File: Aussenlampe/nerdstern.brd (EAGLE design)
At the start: 60 x 50 mm, 14 parts, among them K1 G6RS

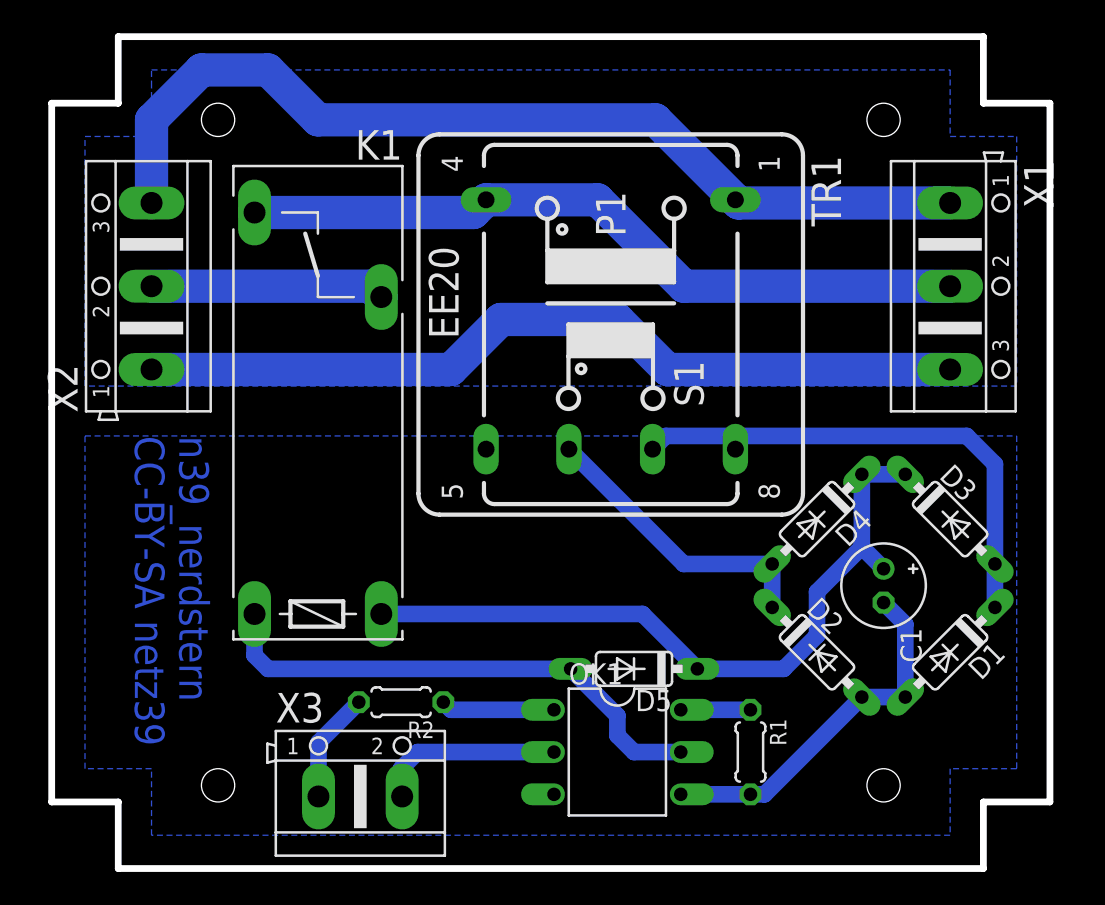
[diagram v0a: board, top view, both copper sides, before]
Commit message: modified .gitignore
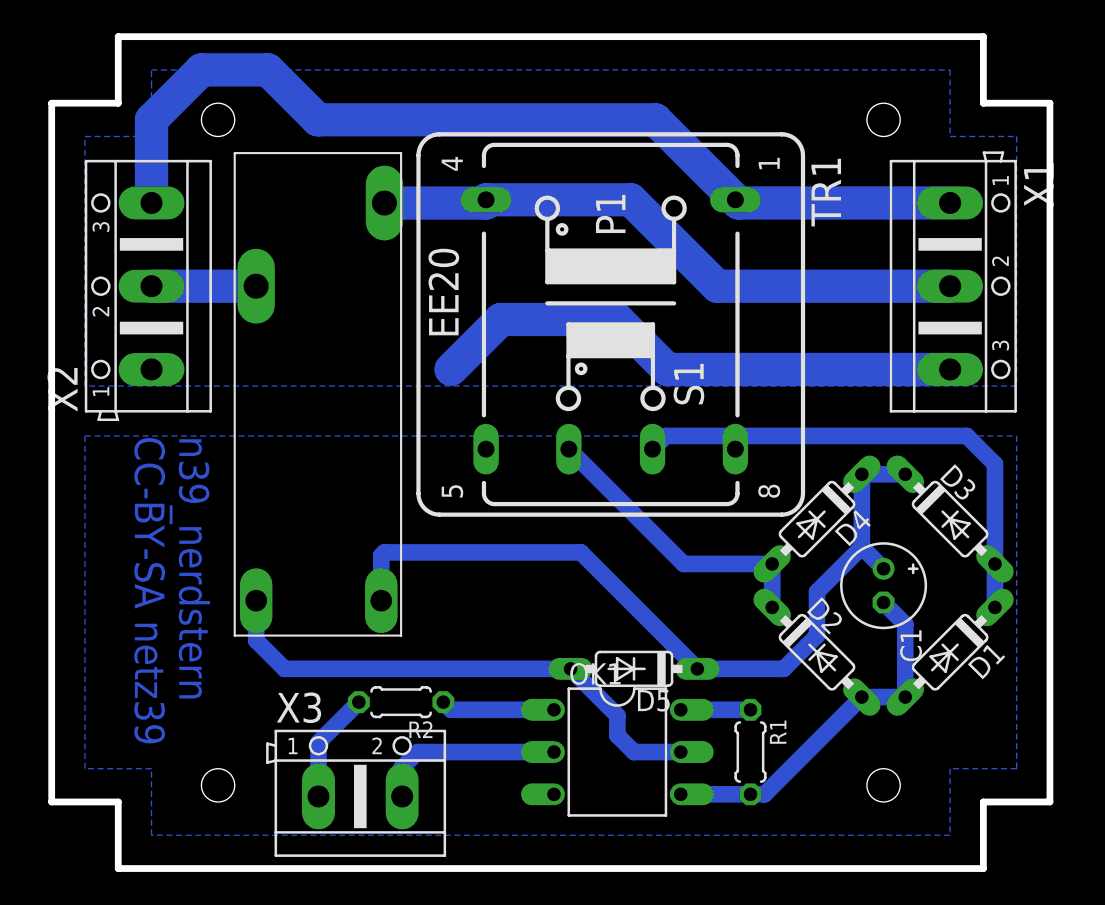
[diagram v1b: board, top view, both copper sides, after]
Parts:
- removed K1: G6RS, relay:G6RS
- added U$1: JS_05_MN_KT, n39:JS_05_MN_KT
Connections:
- removed net N$12: D5.A, K1.2, OK1.5
- new net N$6: D5.A, OK1.5, U$1.P$2
- net N$1: now also U$1.P$4; no longer K1.S
- net N$2: now also U$1.P$3; no longer K1.P
- net N$5: now also U$1.P$1; no longer K1.1
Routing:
- net N$6: track 0.00 -> 31.4 mm
- net N$12: track 31.2 -> 0.00 mm
- net GND2: track 50.5 -> 32.5 mm
- net N$1: track 44.3 -> 36.3 mm
- net N$2: track 14.1 -> 6.29 mm
- net N$5: track 43.7 -> 48.0 mm
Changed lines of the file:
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@@
 <layer number="27" name="tValues" color="7" fill="1" visible="yes" active="yes"/>
 <layer number="28" name="bValues" color="7" fill="1" visible="yes" active="yes"/>
-<layer number="29" name="tStop" color="7" fill="3" visible="no" active="yes"/>
-<layer number="30" name="bStop" color="7" fill="6" visible="no" active="yes"/>
-<layer number="31" name="tCream" color="7" fill="4" visible="no" active="yes"/>
-<layer number="32" name="bCream" color="7" fill="5" visible="no" active="yes"/>
-<layer number="33" name="tFinish" color="6" fill="3" visible="no" active="yes"/>
-<layer number="34" name="bFinish" color="6" fill="6" visible="no" active="yes"/>
-<layer number="35" name="tGlue" color="7" fill="4" visible="no" active="yes"/>
-<layer number="36" name="bGlue" color="7" fill="5" visible="no" active="yes"/>
-<layer number="37" name="tTest" color="7" fill="1" visible="no" active="yes"/>
-<layer number="38" name="bTest" color="7" fill="1" visible="no" active="yes"/>
-<layer number="39" name="tKeepout" color="4" fill="11" visible="no" active="yes"/>
-<layer number="40" name="bKeepout" color="1" fill="11" visible="no" active="yes"/>
-<layer number="41" name="tRestrict" color="4" fill="10" visible="no" active="yes"/>
-<layer number="42" name="bRestrict" color="1" fill="10" visible="no" active="yes"/>
-<layer number="43" name="vRestrict" color="2" fill="10" visible="no" active="yes"/>
+<layer number="29" name="tStop" color="7" fill="3" visible="yes" active="yes"/>
+<layer number="30" name="bStop" color="7" fill="6" visible="yes" active="yes"/>
+<layer number="31" name="tCream" color="7" fill="4" visible="yes" active="yes"/>
+<layer number="32" name="bCream" color="7" fill="5" visible="yes" active="yes"/>
+<layer number="33" name="tFinish" color="6" fill="3" visible="yes" active="yes"/>
+<layer number="34" name="bFinish" color="6" fill="6" visible="yes" active="yes"/>
+<layer number="35" name="tGlue" color="7" fill="4" visible="yes" active="yes"/>
+<layer number="36" name="bGlue" color="7" fill="5" visible="yes" active="yes"/>
+<layer number="37" name="tTest" color="7" fill="1" visible="yes" active="yes"/>
+<layer number="38" name="bTest" color="7" fill="1" visible="yes" active="yes"/>
+<layer number="39" name="tKeepout" color="4" fill="11" visible="yes" active="yes"/>
+<layer number="40" name="bKeepout" color="1" fill="11" visible="yes" active="yes"/>
+<layer number="41" name="tRestrict" color="4" fill="10" visible="yes" active="yes"/>
+<layer number="42" name="bRestrict" color="1" fill="10" visible="yes" active="yes"/>
+<layer number="43" name="vRestrict" color="2" fill="10" visible="yes" active="yes"/>
 <layer number="44" name="Drills" color="7" fill="1" visible="yes" active="yes"/>
 <layer number="45" name="Holes" color="7" fill="1" visible="yes" active="yes"/>
-<layer number="46" name="Milling" color="3" fill="1" visible="no" active="yes"/>
+<layer number="46" name="Milling" color="3" fill="1" visible="yes" active="yes"/>
 <layer number="47" name="Measures" color="7" fill="1" visible="yes" active="yes"/>
 <layer number="48" name="Document" color="7" fill="1" visible="yes" active="yes"/>
@@
 <element name="D4" library="diode" package="DO35-7" value="1N4148" x="46" y="21" rot="R225"/>
 <element name="C1" library="rcl" package="E2-5" value="33u" x="50" y="17" rot="R270"/>
-<element name="K1" library="relay" package="G6RS" value="G6RS" x="16" y="28" rot="R90">
-<attribute name="OC_NEWARK" value="unknown" x="16" y="28" size="1.778" layer="27" rot="R90" display="off"/>
-<attribute name="MPN" value="" x="16" y="28" size="1.778" layer="27" rot="R90" display="off"/>
-<attribute name="MF" value="" x="16" y="28" size="1.778" layer="27" rot="R90" display="off"/>
-<attribute name="OC_FARNELL" value="unknown" x="16" y="28" size="1.778" layer="27" rot="R90" display="off"/>
-</element>
 <element name="X1" library="con-ptr500" package="AK500/3" value="" x="54" y="35" rot="R270">
 <attribute name="OC_NEWARK" value="unknown" x="54" y="35" size="1.778" layer="27" rot="R270" display="off"/>
@@
 <element name="R2" library="rcl" package="0204/5" value="1K" x="21" y="10" rot="R180"/>
 <element name="D5" library="diode" package="DO35-7" value="1N4001" x="35" y="12" rot="R180"/>
+<element name="U$1" library="n39" package="JS_05_MN_KT" value="JS_05_MN_KT" x="21" y="14" rot="R90"/>
 </elements>
 <signals>
@@
 <contactref element="X1" pad="2"/>
 <contactref element="TR1" pad="4"/>
-<contactref element="K1" pad="S"/>
-<wire x1="12.19" y1="39.43" x2="25.344" y2="39.43" width="2" layer="16"/>
-<wire x1="25.344" y1="39.43" x2="26.107" y2="40.193" width="2" layer="16"/>
-<wire x1="26.107" y1="40.193" x2="32.807" y2="40.193" width="2" layer="16"/>
-<wire x1="32.807" y1="40.193" x2="38" y2="35" width="2" layer="16"/>
-<wire x1="38" y1="35" x2="54" y2="35" width="2" layer="16"/>
+<contactref element="U$1" pad="P$4"/>
+<wire x1="20" y1="40" x2="26.107" y2="40" width="2" layer="16"/>
+<wire x1="26.107" y1="40" x2="26.107" y2="40.193" width="2" layer="16"/>
+<wire x1="26.107" y1="40.193" x2="34.807" y2="40.193" width="2" layer="16"/>
+<wire x1="34.807" y1="40.193" x2="40" y2="35" width="2" layer="16"/>
+<wire x1="40" y1="35" x2="54" y2="35" width="2" layer="16"/>
 </signal>
 <signal name="N$2">
-<contactref element="K1" pad="P"/>
 <contactref element="X2" pad="2"/>
-<wire x1="6" y1="35" x2="19.16" y2="35" width="2" layer="16"/>
-<wire x1="19.16" y1="35" x2="19.81" y2="34.35" width="2" layer="16"/>
+<contactref element="U$1" pad="P$3"/>
+<wire x1="6" y1="35" x2="12.29" y2="35" width="2" layer="16"/>
 </signal>
 <signal name="N$3">
@@
 </signal>
 <signal name="N$5">
-<contactref element="K1" pad="1"/>
 <contactref element="C1" pad="+"/>
 <contactref element="D3" pad="C"/>
@@
 <wire x1="48.694075" y1="19.321925" x2="50" y2="18.016" width="1" layer="16"/>
 <contactref element="D5" pad="C"/>
-<wire x1="19.81" y1="15.3" x2="35.51" y2="15.3" width="1" layer="16"/>
-<wire x1="35.51" y1="15.3" x2="38.81" y2="12" width="1" layer="16"/>
 <wire x1="38.81" y1="12" x2="44" y2="12" width="1" layer="16"/>
 <wire x1="44" y1="12" x2="46" y2="14" width="1" layer="16"/>
 <wire x1="46" y1="14" x2="46" y2="16.62785" width="1" layer="16"/>
 <wire x1="46" y1="16.62785" x2="48.694075" y2="19.321925" width="1" layer="16"/>
+<contactref element="U$1" pad="P$1"/>
+<wire x1="19.81" y1="16.1" x2="19.81" y2="18.81" width="1" layer="16"/>
+<wire x1="19.81" y1="18.81" x2="20" y2="19" width="1" layer="16"/>
+<wire x1="20" y1="19" x2="31.81" y2="19" width="1" layer="16"/>
+<wire x1="31.81" y1="19" x2="38.81" y2="12" width="1" layer="16"/>
 </signal>
 <signal name="GND">
@@
 <signal name="GND2">
 <contactref element="X1" pad="3"/>
-<contactref element="X2" pad="1"/>
-<wire x1="6" y1="29.9962" x2="23.9962" y2="29.9962" width="2" layer="16"/>
 <wire x1="23.9962" y1="29.9962" x2="27" y2="33" width="2" layer="16"/>
 <wire x1="27" y1="33" x2="34" y2="33" width="2" layer="16"/>
@@
 <vertex x="6" y="47"/>
 </polygon>
+<contactref element="X2" pad="1"/>
 </signal>
 <signal name="N$10">
@@
 <wire x1="37.81" y1="9.54" x2="42" y2="9.54" width="1" layer="16"/>
 </signal>
-<signal name="N$12">
-<contactref element="K1" pad="2"/>
+<signal name="N$15">
+<contactref element="X3" pad="1"/>
+<contactref element="R2" pad="2"/>
+<wire x1="16.0354" y1="4.33" x2="16.0354" y2="7.5754" width="1" layer="16"/>
+<wire x1="16.0354" y1="7.5754" x2="18.46" y2="10" width="1" layer="16"/>
+</signal>
+<signal name="N$6">
+<contactref element="U$1" pad="P$2"/>
 <contactref element="OK1" pad="5"/>
 <contactref element="D5" pad="A"/>
@@
 <wire x1="34" y1="8" x2="34" y2="9.19" width="1" layer="16"/>
 <wire x1="34" y1="9.19" x2="31.19" y2="12" width="1" layer="16"/>
-<wire x1="31.19" y1="12" x2="13" y2="12" width="1" layer="16"/>
-<wire x1="13" y1="12" x2="12.19" y2="12.81" width="1" layer="16"/>
-<wire x1="12.19" y1="12.81" x2="12.19" y2="15.3" width="1" layer="16"/>
-</signal>
-<signal name="N$15">
-<contactref element="X3" pad="1"/>
-<contactref element="R2" pad="2"/>
-<wire x1="16.0354" y1="4.33" x2="16.0354" y2="7.5754" width="1" layer="16"/>
-<wire x1="16.0354" y1="7.5754" x2="18.46" y2="10" width="1" layer="16"/>
+<wire x1="31.19" y1="12" x2="14" y2="12" width="1" layer="16"/>
+<wire x1="14" y1="12" x2="12.29" y2="13.71" width="1" layer="16"/>
+<wire x1="12.29" y1="13.71" x2="12.29" y2="16.1" width="1" layer="16"/>
 </signal>
 </signals>
